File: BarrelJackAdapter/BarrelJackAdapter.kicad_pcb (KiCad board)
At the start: 2 copper layers, 6 parts, among them J1 Barrel_Jack_Switch, J2 Conn_01x03, J4 Conn_01x03, U1 L7805

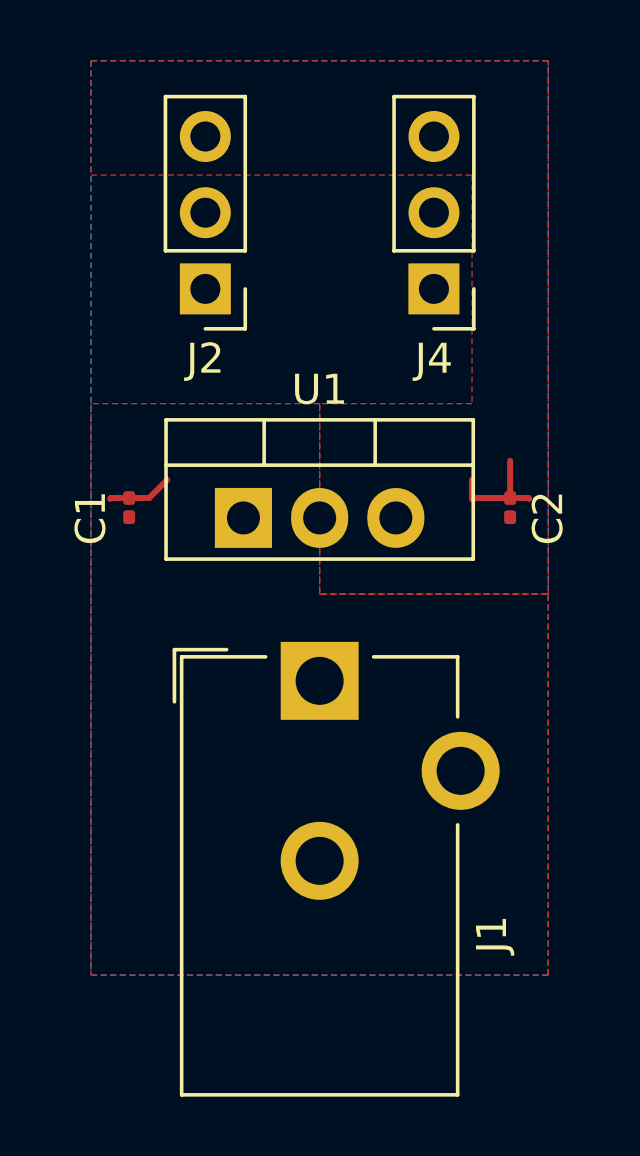
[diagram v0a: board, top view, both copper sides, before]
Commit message: Small board to hold a barrel jack on a breadboard.  Through holes for a T0-223 regulator (eg an L7805)
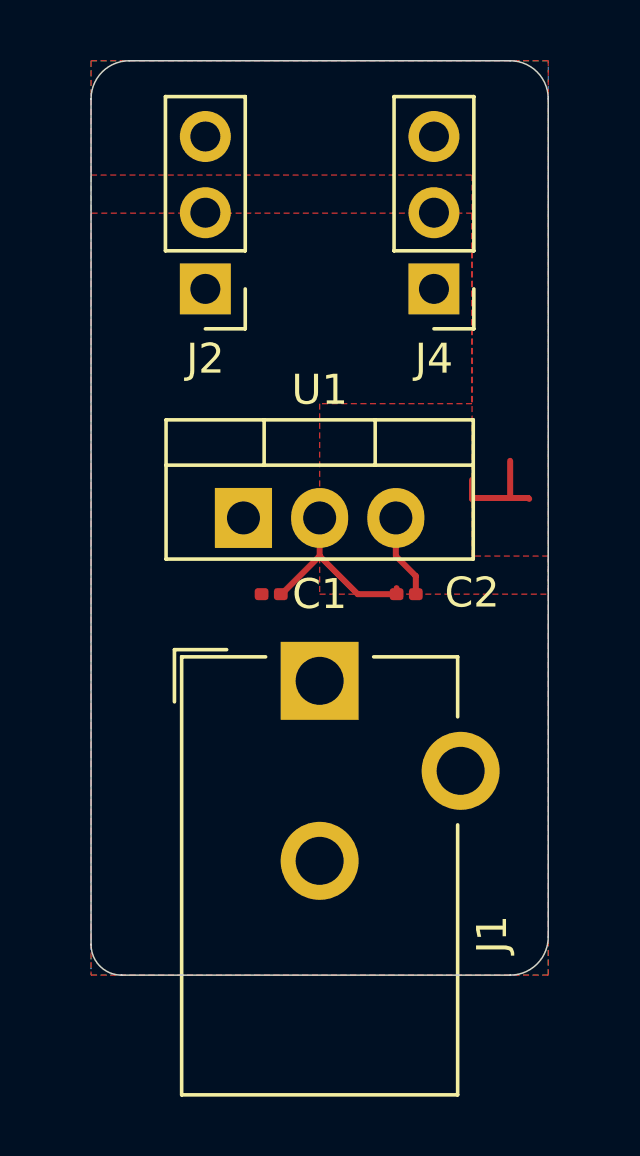
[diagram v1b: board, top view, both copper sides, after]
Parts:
- moved C1 5.54 mm to (182.5, 67.3), turned to 0 degrees
- moved C2 4.51 mm to (187.0, 67.3), turned to 180 degrees
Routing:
- net GND: track 0.00 -> 6.61 mm
- net +5V: track 3.80 -> 6.62 mm
- net +9V: track 2.17 -> 0.00 mm
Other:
- board outline added: 15.2 x 30.5 mm

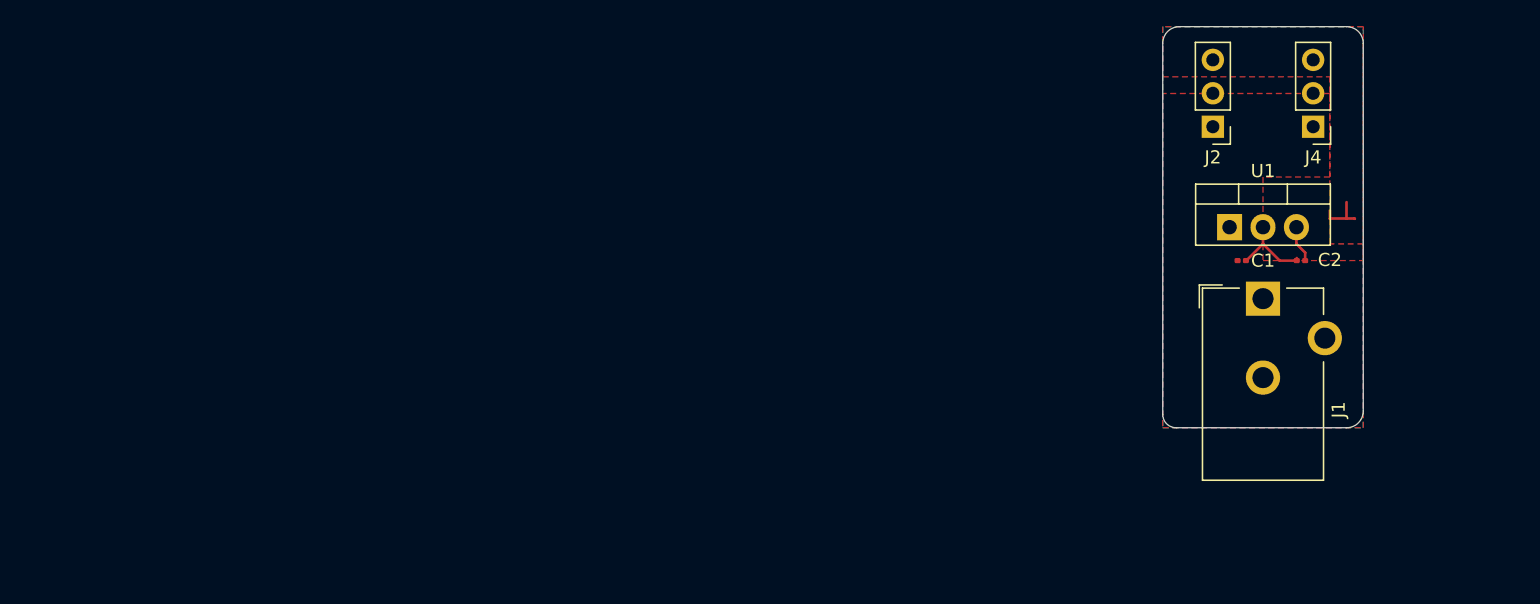
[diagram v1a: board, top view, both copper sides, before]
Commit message: new rev of barrel jack.  Now with more complication!
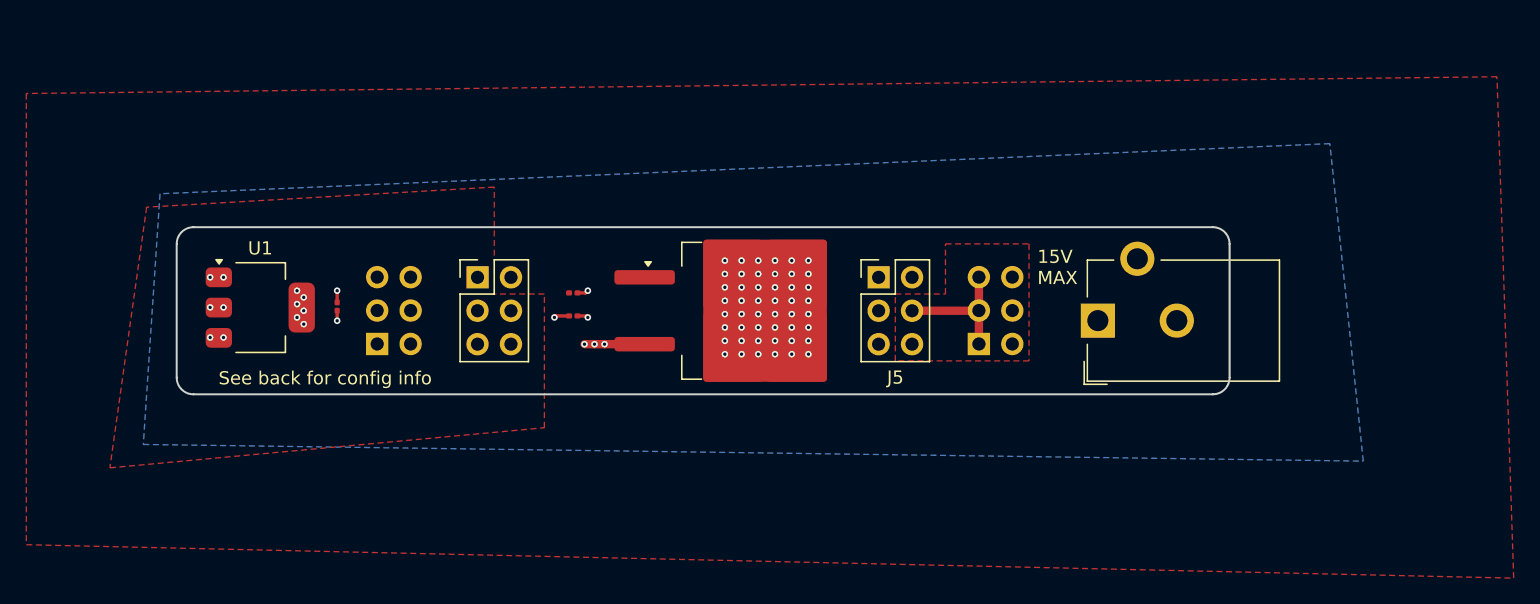
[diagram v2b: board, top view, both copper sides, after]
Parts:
- added C3: 10u, Capacitor_SMD:C_0201_0603Metric, F.Cu at (113.8, 70.8)
- added J3: Conn_02x03_Counter_Clockwise, Connector_PinHeader_2.54mm:PinHeader_2x03_P2.54mm_Vertical, F.Cu at (124.5, 68.6)
- added J5: Conn_02x03_Counter_Clockwise, Connector_PinHeader_2.54mm:PinHeader_2x03_P2.54mm_Vertical, F.Cu at (154.9, 68.6)
- added U2: L7805, Package_TO_SOT_SMD:TO-263-2, F.Cu at (144.8, 71.1)
- J2, J4: value Conn_01x03 -> Conn_02x03_Counter_Clockwise; footprint Connector_PinHeader_2.54mm:PinHeader_1x03_P2.54mm_Vertical -> Connector_PinHeader_2.54mm:PinHeader_2x03_P2.54mm_Vertical; moved to B.Cu
- U1: value L7805 -> LD1117S33TR_SOT223; footprint Package_TO_SOT_THT:TO-220-3_Vertical -> Package_TO_SOT_SMD:SOT-223-3_TabPin2
- moved U1 73.9 mm to (108.0, 70.9)
- moved J2 65.6 mm to (116.8, 73.6), turned to 0 degrees
- moved C2 55.5 mm to (131.7, 71.5), turned to 0 degrees
- moved C1 50.9 mm to (131.7, 69.8)
- moved J4 30.3 mm to (162.6, 73.6), turned to 0 degrees
- moved J1 12.7 mm to (171.6, 71.9), turned to 90 degrees
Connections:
- J2 pad 1: +9V -> /Vleft
- J2 pad 3: +5V -> /Vleft
- J4 pad 1: +9V -> /Vright
- J4 pad 3: +5V -> /Vright
- U1 pad 1: +9V -> GND
- U1 pad 2: GND -> +3.3V
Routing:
- net /Vright: track 0.00 -> 10.2 mm
- net GND: track 6.61 -> 2.57 mm, vias 0 -> 53
- net +5V: track 6.62 -> 5.73 mm, vias 0 -> 6
- net +3.3V: track 0.00 -> 0.76 mm, vias 0 -> 9
- added copper zone on In2.Cu, net +3.3V
- added copper zone on In1.Cu, net +5V
- added copper zone on F.Cu, net /Vleft
- added copper zone on F.Cu, net /Vright
- removed copper zone on F.Cu, net +5V
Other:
- board size 15.2 x 30.5 mm -> 80 x 12.7 mm
- copper layers 2 -> 4
- board text added: "15V MAX"
- board text added: "3V"
- board text added: "5V"
- board text added: "9V"
- board text added: "Jumper Positions"
- board text added: "See back for config info"

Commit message: V1.0 artwork
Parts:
- added G***: LOGO, QRCodes:BarrelJack, B.Cu at (108.0, 70.5)
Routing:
- added copper zone on In1.Cu, net GND
- added copper zone on In2.Cu, net GND
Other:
- board text added: "Barrel Adapter V1.0"

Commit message: V1.0 now more silk!
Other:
- board text added: "Copyright 2024, Tad Truex"
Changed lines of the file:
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@@
 			(pintype "passive")
 		)
-		(model "${KICAD8_3DMODEL_DIR}/Connector_BarrelJack.3dshapes/BarrelJack_CUI_PJ-102AH_Horizontal.wrl"
+		(model "${KICAD_3DMODEL_DIR}/Connector_BarrelJack.3dshapes/BarrelJack_CUI_PJ-102AH_Horizontal.wrl"
 			(offset
 				(xyz 0 0 0)
@@
 			(rotate
 				(xyz 0 0 0)
+			)
+		)
+		(model "${KICAD8_3DMODEL_DIR}/Connector_BarrelJack.3dshapes/BarrelJack_Horizontal.step"
+			(offset
+				(xyz 0 0 0)
+			)
+			(scale
+				(xyz 1 1 1)
+			)
+			(rotate
+				(xyz 0 0 -90)
 			)
 		)
@@
 		)
 	)
-	(gr_text "9V"
-		(at 142.875 71.755 -90)
+	(gr_text "Copyright 2024, Tad Truex"
+		(at 177.8 76.835 0)
 		(layer "B.SilkS")
 		(effects
@@
 		)
 	)
+	(gr_text "9V"
+		(at 142.875 71.755 -90)
+		(layer "B.SilkS")
+		(effects
+			(font
+				(size 1 1)
+				(thickness 0.15)
+			)
+			(justify left bottom mirror)
+		)
+	)
 	(gr_text "See back for config info"
-		(at 104.775 76.835 0)
+		(at 114.3 76.835 0)
 		(layer "F.SilkS")
 		(effects
@@
 		)
 	)
+	(gr_text "Barrel Adapter V1.0"
+		(at 114.935 66.675 0)
+		(layer "F.SilkS")
+		(effects
+			(font
+				(size 1 1)
+				(thickness 0.15)
+			)
+			(justify left bottom)
+		)
+	)
 	(gr_text "15V\nMAX"
 		(at 167.005 69.215 0)
@@
 		(effects
 			(font
-				(size 1 1)
-				(thickness 0.15)
-			)
-			(justify left bottom)
-		)
-	)
-	(gr_text "Barrel Adapter V1.0"
-		(at 165.1 76.2 0)
-		(layer "Edge.Cuts")
-		(effects
-			(font
